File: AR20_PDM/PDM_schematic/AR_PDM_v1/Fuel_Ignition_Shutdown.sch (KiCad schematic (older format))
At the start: 16 parts

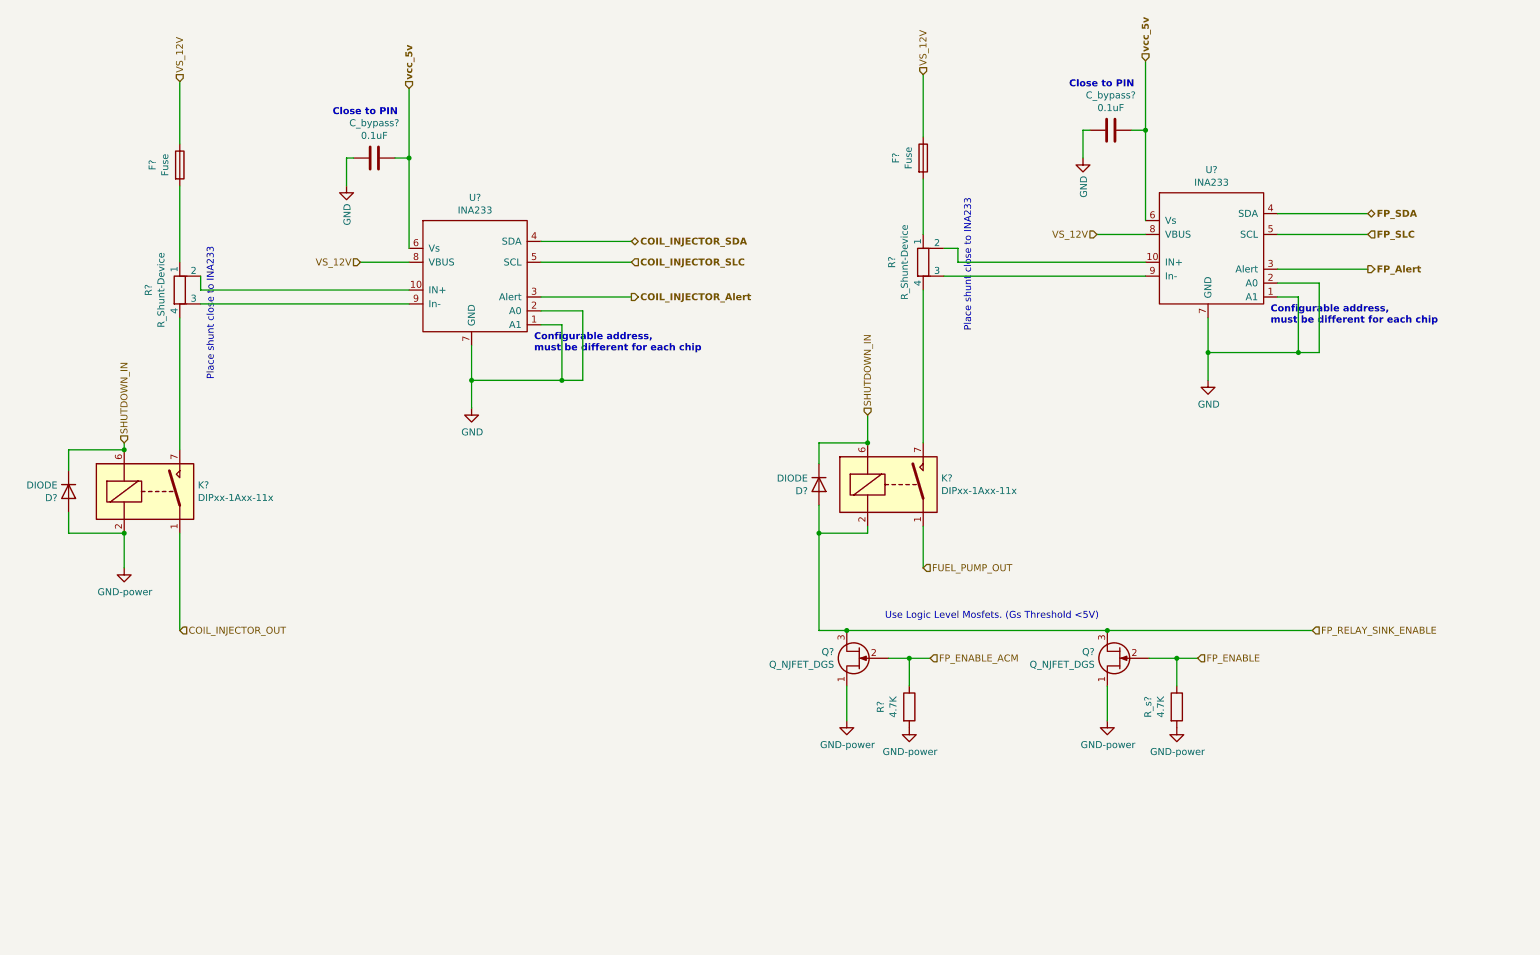
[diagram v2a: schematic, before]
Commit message: Major Schematics changes-work in progress
- Added rest of the phases
- Corrected pin names, and began to connect everything
- Began mapping the connectors, Pin-out not yet verified for all connectors
- Began mapping of user interface (Led indicators)
- INA233 now senses OUT voltage on mosfets instead of main 12Volt
- Added extra decoupling capacitors
Known things to fix:
- AUX inputs activation method, and a disconnect switch on phase 1-7 (mosfets)
- Rest of the user interface
- Find correct plugs for the system
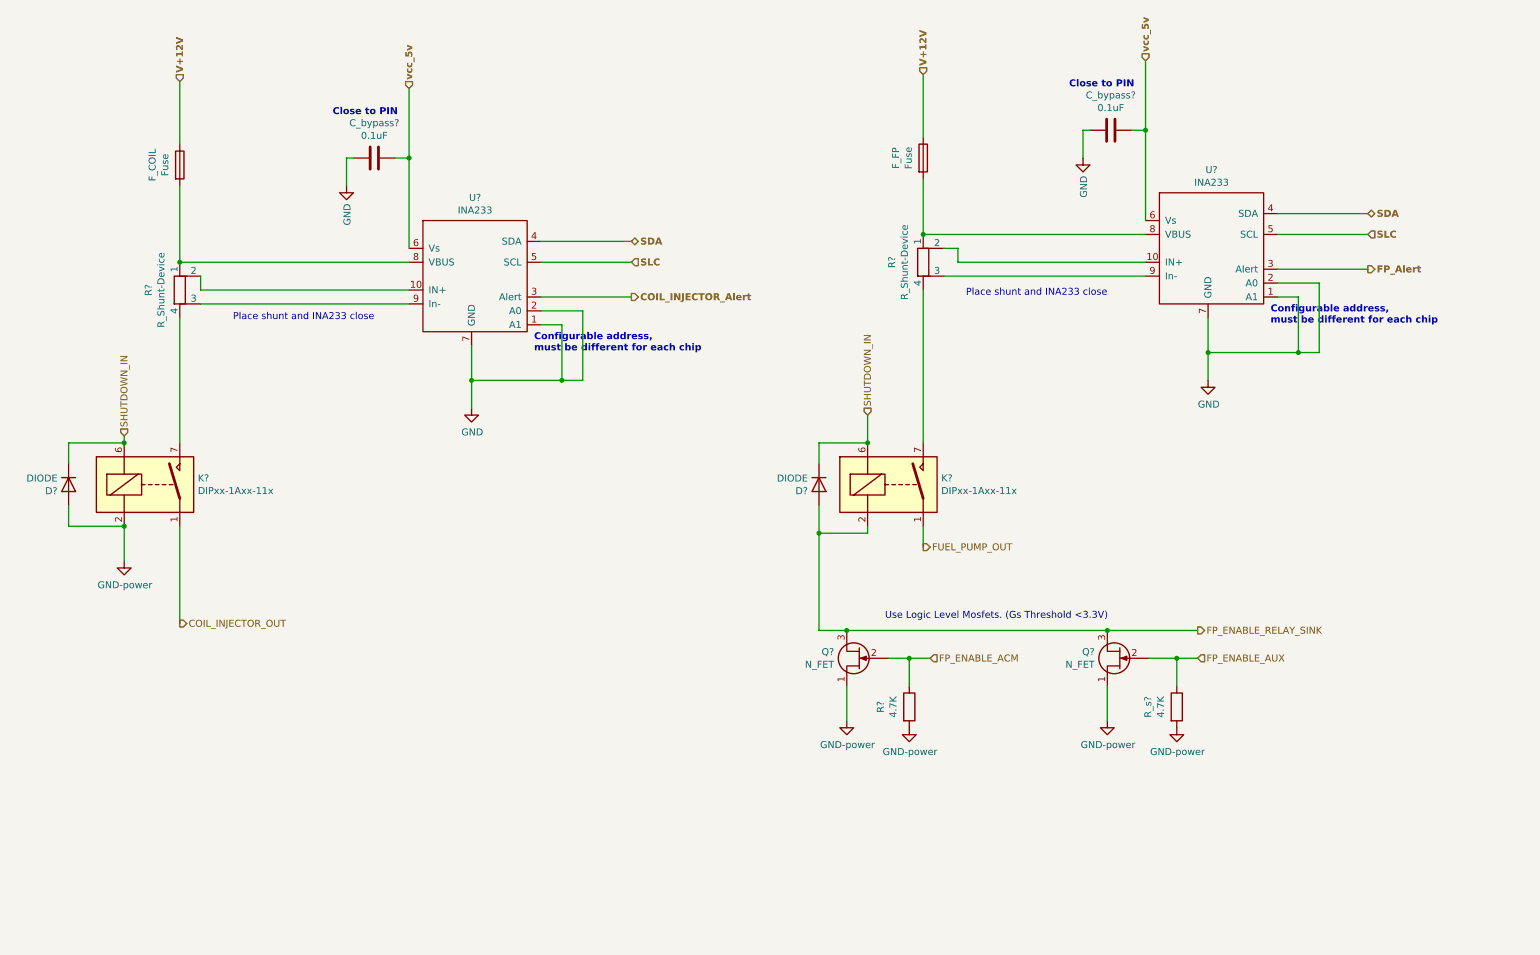
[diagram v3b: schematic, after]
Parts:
- Q? (x2): value Q_NJFET_DGS -> N_FET
- gave numbers to parts that had none: 2
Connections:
- net FP_SDA is gone; now on net SDA: U?.4 (SDA)
- net FP_SLC is gone; now on net SLC: U?.5 (SCL)
- net at F_COIL.2, R?.1: now also U?.8 (VBUS)
- net at F_FP.2, R?.1: now also U?.8 (VBUS)
- net COIL_INJECTOR_SDA renamed SDA
- net COIL_INJECTOR_SLC renamed SLC
- net FP_ENABLE renamed FP_ENABLE_AUX
- net FP_RELAY_SINK_ENABLE renamed FP_ENABLE_RELAY_SINK
- net VS_12V renamed V+12V
- net V+12V: no longer U?.8 (VBUS), U?.8 (VBUS)
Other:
- note added: "Place shunt and INA233 close \n"
- note added: "Use Logic Level Mosfets. (Gs Threshold <3.3V)"
- note removed: "Place shunt close to INA233\n"
- note removed: "Use Logic Level Mosfets. (Gs Threshold <5V)"
- moved on the sheet: D?, K?
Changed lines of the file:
@@
 $Descr A4 11693 8268
 encoding utf-8
-Sheet 4 6
+Sheet 2 11
 Title ""
 Date ""
@@
 Comment4 ""
 $EndDescr
-Text HLabel 7350 4550 2    50   Input ~ 0
+Text HLabel 7350 4400 2    50   Output ~ 0
 FUEL_PUMP_OUT
 $Comp
@@
 $EndComp
 Wire Wire Line
-	7350 4250 7350 4550
+	7350 4250 7350 4400
 $Comp
 L Device:Q_NJFET_DGS Q?
@@
 P 6900 5200
 F 0 "Q?" H 7091 5154 50  0000 L CNN
-F 1 "Q_NJFET_DGS" H 7091 5245 50  0000 L CNN
+F 1 "N_FET" H 7091 5245 50  0000 L CNN
 F 2 "" H 7100 5300 50  0001 C CNN
 F 3 "~" H 6900 5200 50  0001 C CNN
@@
 P 8775 5200
 F 0 "Q?" H 8966 5154 50  0000 L CNN
-F 1 "Q_NJFET_DGS" H 8966 5245 50  0000 L CNN
+F 1 "N_FET" H 8966 5245 50  0000 L CNN
 F 2 "" H 8975 5300 50  0001 C CNN
 F 3 "~" H 8775 5200 50  0001 C CNN
@@
 Wire Wire Line
 	6600 4300 6600 5000
-Text HLabel 2000 5000 2    50   Input ~ 0
+Text HLabel 2000 4950 2    50   Output ~ 0
 COIL_INJECTOR_OUT
 $Comp
@@
 	1    0    0    -1
 $EndComp
-Text HLabel 7350 1000 1    50   Input ~ 0
-VS_12V
-$Comp
-L Device:Fuse F?
+$Comp
+L Device:Fuse F_FP
 U 1 1 5DDF15AA
 P 7350 1600
-F 0 "F?" V 7153 1600 50  0000 C CNN
+F 0 "F_FP" V 7153 1600 50  0000 C CNN
 F 1 "Fuse" V 7244 1600 50  0000 C CNN
 F 2 "" V 7280 1600 50  0001 C CNN
@@
 FP_Alert
 Text HLabel 10550 2000 2    50   BiDi ~ 10
-FP_SDA
+SDA
 Text HLabel 10550 2150 2    50   Input ~ 10
-FP_SLC
+SLC
 Text Notes 8400 1100 0    50   ~ 10
 Close to PIN
@@
 Close to PIN
 Text HLabel 5250 2350 2    50   Input ~ 10
-COIL_INJECTOR_SLC
+SLC
 Text HLabel 5250 2200 2    50   BiDi ~ 10
-COIL_INJECTOR_SDA
+SDA
 Text HLabel 5250 2600 2    50   Output ~ 10
 COIL_INJECTOR_Alert
@@
 L Relay:DIPxx-1Axx-11x K?
 U 1 1 5DDBA337
-P 1800 4000
-F 0 "K?" H 2130 4046 50  0000 L CNN
-F 1 "DIPxx-1Axx-11x" H 2130 3955 50  0000 L CNN
-F 2 "Relay_THT:Relay_StandexMeder_DIP_LowProfile" H 2150 3950 50  0001 L CNN
-F 3 "https://standexelectronics.com/wp-content/uploads/datasheet_reed_relay_DIP.pdf" H 1800 4000 50  0001 C CNN
-	1    1800 4000
+P 1800 3950
+F 0 "K?" H 2130 3996 50  0000 L CNN
+F 1 "DIPxx-1Axx-11x" H 2130 3905 50  0000 L CNN
+F 2 "Relay_THT:Relay_StandexMeder_DIP_LowProfile" H 2150 3900 50  0001 L CNN
+F 3 "https://standexelectronics.com/wp-content/uploads/datasheet_reed_relay_DIP.pdf" H 1800 3950 50  0001 C CNN
+	1    1800 3950
 	1    0    0    -1
 $EndComp
@@
 L AR20_PDM_v1-rescue:GND-power #PWR?
 U 1 1 5DDBDA4F
-P 1600 4550
-F 0 "#PWR?" H 1600 4300 50  0001 C CNN
-F 1 "GND-power" H 1605 4377 50  0000 C CNN
-F 2 "" H 1600 4550 50  0001 C CNN
-F 3 "" H 1600 4550 50  0001 C CNN
-	1    1600 4550
-	1    0    0    -1
-$EndComp
-Wire Wire Line
-	1600 4550 1600 4300
-Wire Wire Line
-	2000 4300 2000 5000
-Wire Wire Line
-	1600 3700 1600 3650
-Text HLabel 1600 3650 1    50   Input ~ 0
+P 1600 4500
+F 0 "#PWR?" H 1600 4250 50  0001 C CNN
+F 1 "GND-power" H 1605 4327 50  0000 C CNN
+F 2 "" H 1600 4500 50  0001 C CNN
+F 3 "" H 1600 4500 50  0001 C CNN
+	1    1600 4500
+	1    0    0    -1
+$EndComp
+Wire Wire Line
+	1600 4500 1600 4250
+Wire Wire Line
+	2000 4250 2000 4950
+Wire Wire Line
+	1600 3650 1600 3600
+Text HLabel 1600 3600 1    50   Input ~ 0
 SHUTDOWN_IN
 Wire Wire Line
-	1600 3700 1200 3700
-Connection ~ 1600 3700
-Wire Wire Line
-	1200 4300 1600 4300
-Connection ~ 1600 4300
-Wire Wire Line
-	1200 4150 1200 4300
-Wire Wire Line
-	1200 3700 1200 3850
+	1600 3650 1200 3650
+Connection ~ 1600 3650
+Wire Wire Line
+	1200 4250 1600 4250
+Connection ~ 1600 4250
+Wire Wire Line
+	1200 4100 1200 4250
+Wire Wire Line
+	1200 3650 1200 3800
 $Comp
 L AR20_PDM_v1-rescue:DIODE-Simulation_SPICE D?
 U 1 1 5DDCE100
-P 1200 4000
-F 0 "D?" V 1154 4080 50  0000 L CNN
-F 1 "DIODE" V 1245 4080 50  0000 L CNN
-F 2 "" H 1200 4000 50  0001 C CNN
-F 3 "" H 1200 4000 50  0001 C CNN
-F 4 "Y" H 1200 4000 50  0001 L CNN "Spice_Netlist_Enabled"
-F 5 "V" H 1200 4000 50  0001 L CNN "Spice_Primitive"
-	1    1200 4000
+P 1200 3950
+F 0 "D?" V 1154 4030 50  0000 L CNN
+F 1 "DIODE" V 1245 4030 50  0000 L CNN
+F 2 "" H 1200 3950 50  0001 C CNN
+F 3 "" H 1200 3950 50  0001 C CNN
+F 4 "Y" H 1200 3950 50  0001 L CNN "Spice_Netlist_Enabled"
+F 5 "V" H 1200 3950 50  0001 L CNN "Spice_Primitive"
+	1    1200 3950
 	0    -1   -1   0
 $EndComp
@@
 Wire Wire Line
 	7350 1450 7350 1000
-Text HLabel 2000 1050 1    50   Input ~ 0
-VS_12V
-$Comp
-L Device:Fuse F?
+$Comp
+L Device:Fuse F_COIL
 U 1 1 5DE5EBA7
 P 2000 1650
-F 0 "F?" V 1803 1650 50  0000 C CNN
+F 0 "F_COIL" V 1803 1650 50  0000 C CNN
 F 1 "Fuse" V 1894 1650 50  0000 C CNN
 F 2 "" V 1930 1650 50  0001 C CNN
@@
 	2000 1500 2000 1050
 Wire Wire Line
-	2000 2750 2000 3700
+	2000 2750 2000 3650
 Wire Wire Line
 	7350 2550 7350 3650
-Text Notes 2250 3200 1    50   ~ 0
-Place shunt close to INA233\n
-Text Notes 7700 2850 1    50   ~ 0
-Place shunt close to INA233\n
+Text Notes 8675 2600 2    50   ~ 0
+Place shunt and INA233 close \n
 Wire Wire Line
 	2000 1800 2000 2350
-Text HLabel 3300 2350 0    50   Input ~ 0
-VS_12V
-Wire Wire Line
-	3650 2350 3300 2350
 Wire Wire Line
 	7350 1750 7350 2150
-Text HLabel 8600 2150 0    50   Input ~ 0
-VS_12V
-Wire Wire Line
-	8600 2150 8950 2150
 Text HLabel 9325 5200 2    50   Input ~ 0
-FP_ENABLE
+FP_ENABLE_AUX
 Wire Wire Line
 	8975 5200 9175 5200
@@
 Connection ~ 9175 5200
 Connection ~ 8675 5000
-Text HLabel 10150 5000 2    50   Input ~ 0
-FP_RELAY_SINK_ENABLE
-Wire Wire Line
-	8675 5000 10150 5000
+Text HLabel 9325 5000 2    50   Output ~ 0
+FP_ENABLE_RELAY_SINK
+Wire Wire Line
+	8675 5000 9325 5000
 Text Notes 7075 4925 0    50   ~ 0
-Use Logic Level Mosfets. (Gs Threshold <5V)
+Use Logic Level Mosfets. (Gs Threshold <3.3V)
+Wire Wire Line
+	7350 2150 8950 2150
+Connection ~ 7350 2150
+Wire Wire Line
+	2000 2350 3650 2350
+Connection ~ 2000 2350
+Text Notes 3400 2775 2    50   ~ 0
+Place shunt and INA233 close \n
+Text HLabel 2000 1050 1    50   Input ~ 10
+V+12V
+Text HLabel 7350 1000 1    50   Input ~ 10
+V+12V
 $EndSCHEMATC

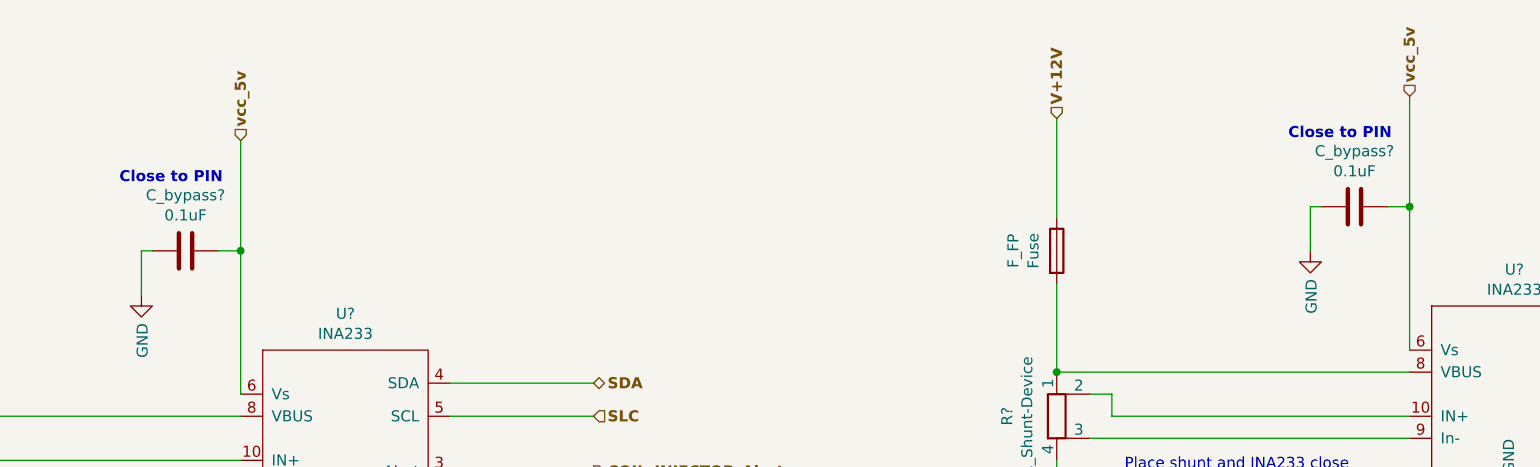
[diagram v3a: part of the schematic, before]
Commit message: Fixed wrong value components and ports, wiring, see discription
- Fixed supply cappacitor value 220 nf to 100nf
- Fixed IN cappacitor value 220 nf to 150 nf
- Fixed out cappacitor value, 220nf to 10 nf
- Made a mux for mosfet sense
- Found a I/O port expander
- Added some and removed some leds
- Fixed all labels, and wired everything up, besides the connectors
- Still missing connector and acm connector pinout.
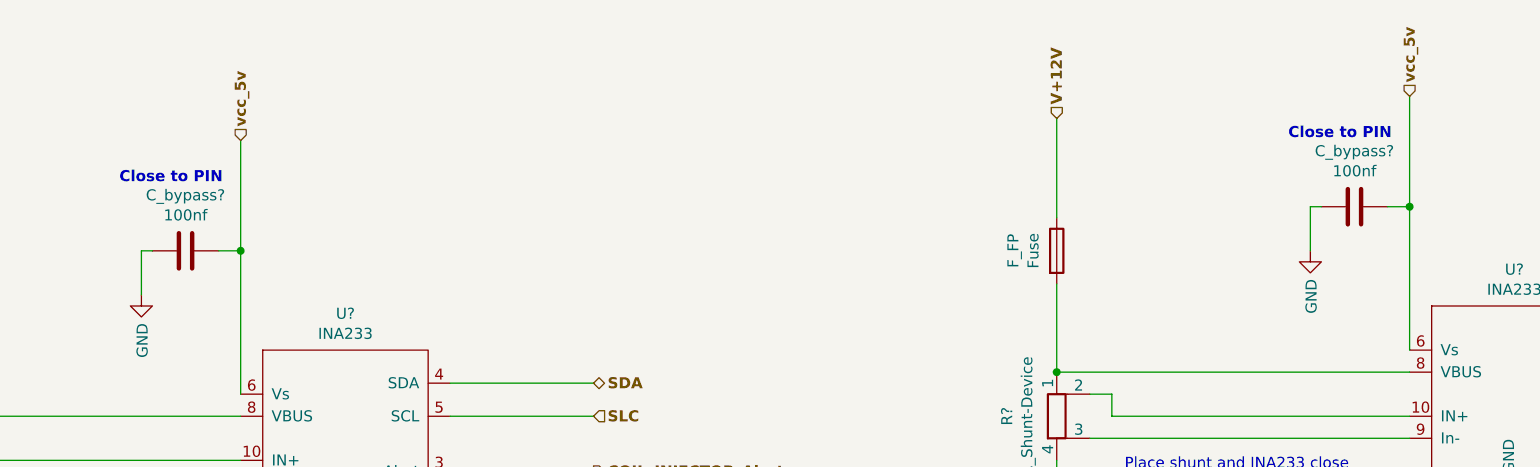
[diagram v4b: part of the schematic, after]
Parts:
- C_bypass? (x2): value 0.1uF -> 100nf
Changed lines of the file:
@@
 $Descr A4 11693 8268
 encoding utf-8
-Sheet 2 11
+Sheet 2 13
 Title ""
 Date ""
@@
 AR Path="/5DA8920B/5DE0EACB" Ref="C_bypass?"  Part="1"
 F 0 "C_bypass?" V 8448 1400 50  0000 C CNN
-F 1 "0.1uF" V 8539 1400 50  0000 C CNN
+F 1 "100nf" V 8539 1400 50  0000 C CNN
 F 2 "" H 8738 1250 50  0001 C CNN
 F 3 "~" H 8700 1400 50  0001 C CNN
@@
 $EndComp
 $Comp
-L AR20_PDM_v1-rescue:C-Device C_bypass?
-U 1 1 5DE077B4
-P 3400 1600
-AR Path="/5DA89415/5DE077B4" Ref="C_bypass?"  Part="1"
-AR Path="/5DA8920B/5DE077B4" Ref="C_bypass?"  Part="1"
-F 0 "C_bypass?" V 3148 1600 50  0000 C CNN
-F 1 "0.1uF" V 3239 1600 50  0000 C CNN
-F 2 "" H 3438 1450 50  0001 C CNN
-F 3 "~" H 3400 1600 50  0001 C CNN
-	1    3400 1600
-	0    1    1    0
-$EndComp
-$Comp
 L Relay:DIPxx-1Axx-11x K?
 U 1 1 5DDBA337
@@
 Text HLabel 7350 1000 1    50   Input ~ 10
 V+12V
+$Comp
+L AR20_PDM_v1-rescue:C-Device C_bypass?
+U 1 1 5DE077B4
+P 3400 1600
+AR Path="/5DA89415/5DE077B4" Ref="C_bypass?"  Part="1"
+AR Path="/5DA8920B/5DE077B4" Ref="C_bypass?"  Part="1"
+F 0 "C_bypass?" V 3148 1600 50  0000 C CNN
+F 1 "100nf" V 3239 1600 50  0000 C CNN
+F 2 "" H 3438 1450 50  0001 C CNN
+F 3 "~" H 3400 1600 50  0001 C CNN
+	1    3400 1600
+	0    1    1    0
+$EndComp
 $EndSCHEMATC
